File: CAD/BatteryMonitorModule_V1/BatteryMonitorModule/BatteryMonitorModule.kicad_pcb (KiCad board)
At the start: 2 copper layers, 74.6 x 74.6 mm, 72 parts, among them J1 J_FAN, J2 QT06ADP83H0000G, J3 J_NFC, J4 J_PANEL, J5 J_UART, J6 Conn_ARM_JTAG_SWD_10, J7 USB-C, K1 G5Q-14-DC12, Q1 AO4407A, Q2 AO4407A, Q3 AO3400A, Q4 MMBT2222A, Q5 2N7002, SW1 BOOT0, SW2 NRST, U1 STM32C071K8T6, U2 AP63203WU-7, U3 INA226AQDGSRQ1

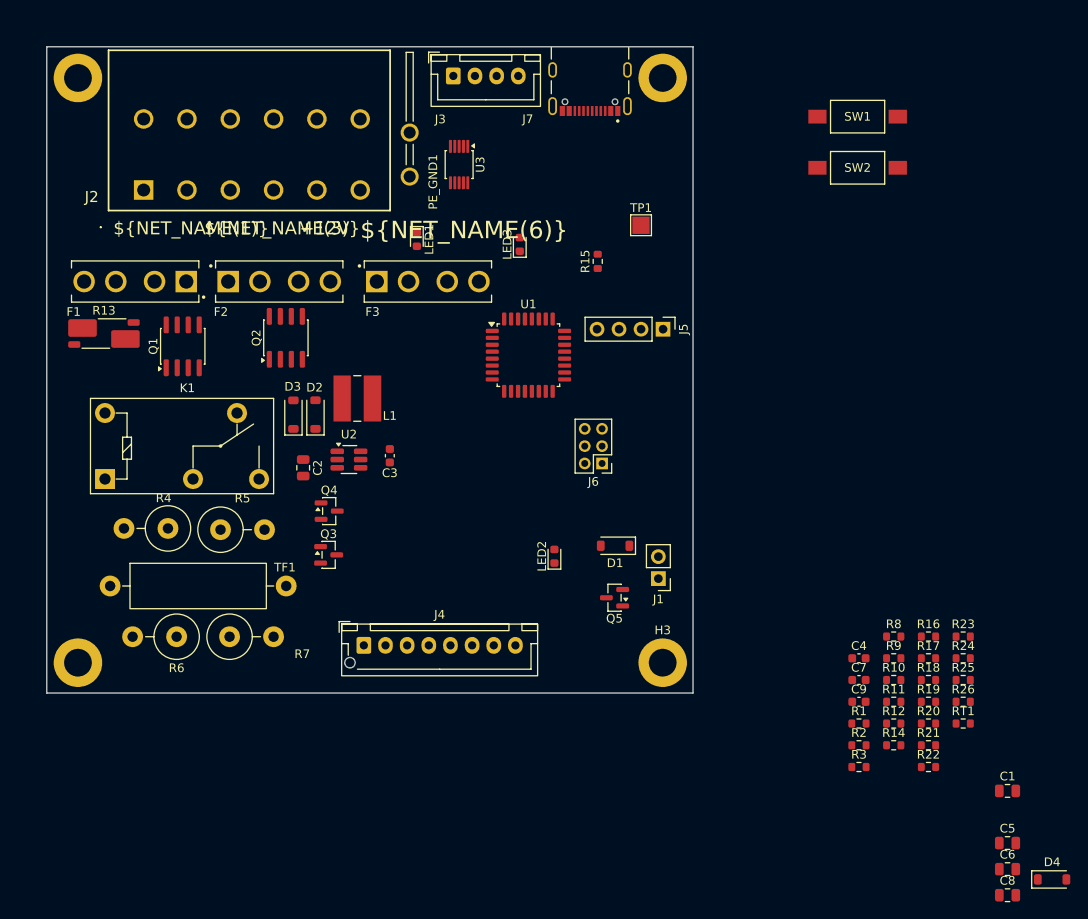
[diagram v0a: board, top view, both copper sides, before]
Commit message: V1 PCB and schematic updates
Co-Authored-By: Claude Opus 4.7 (1M context) <noreply@anthropic.com>
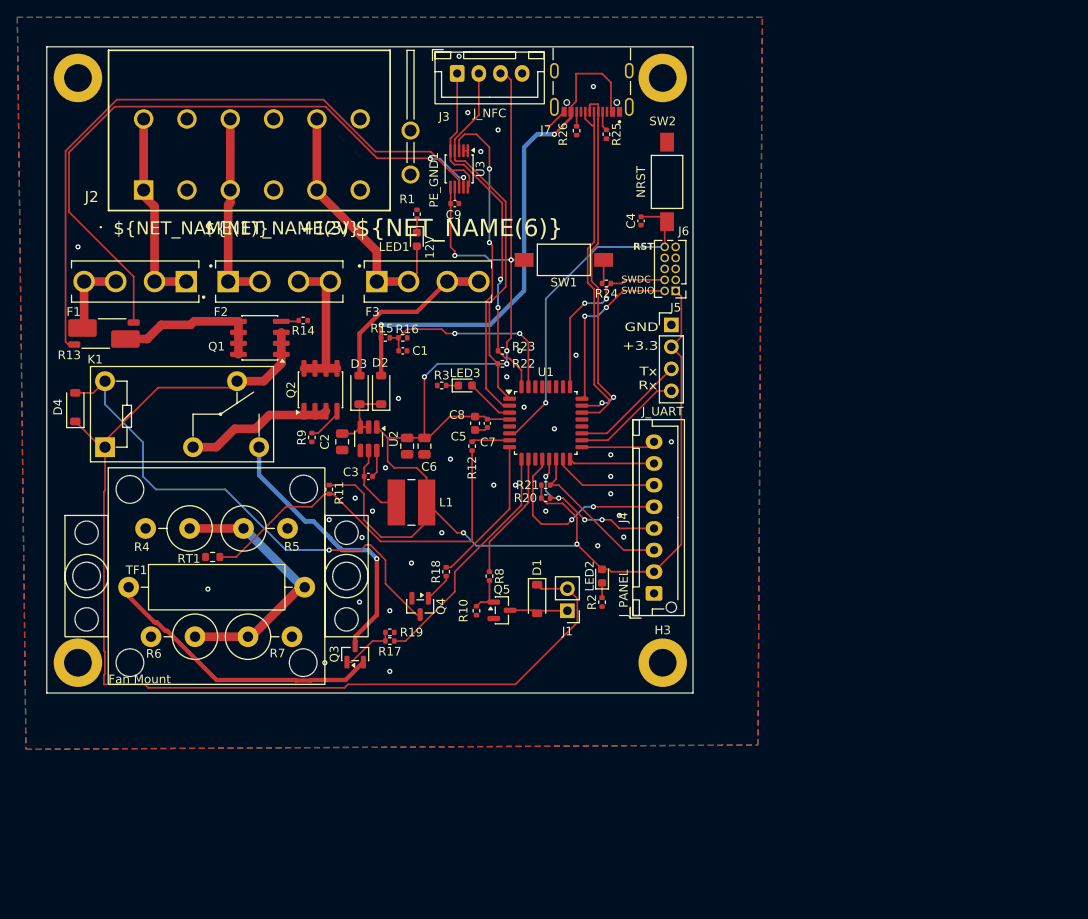
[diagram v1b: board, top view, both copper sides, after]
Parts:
- removed TP1: +3.3V, TestPoint:TestPoint_Pad_2.0x2.0mm
- added H5: Fan1, BatteryMonitorModule_Custom:2510FanOverhead, F.Cu at (45.0, 86.5)
- C1: footprint Capacitor_SMD:C_0805_2012Metric -> Capacitor_SMD:C_0402_1005Metric
- C3, C4, C7, C9: footprint Capacitor_SMD:C_0603_1608Metric -> Capacitor_SMD:C_0402_1005Metric
- C8: footprint Capacitor_SMD:C_0805_2012Metric -> Capacitor_SMD:C_0603_1608Metric
- J6: footprint Connector_PinHeader_2.00mm:PinHeader_2x03_P2.00mm_Vertical -> Connector_PinHeader_1.27mm:PinHeader_2x05_P1.27mm_Vertical
- R1: value 2k -> 10k; footprint Resistor_SMD:R_0603_1608Metric -> Resistor_SMD:R_0402_1005Metric
- R10, R11, R14, R15, R16, R17, R18, R19, R24, R25, R26, R9: footprint Resistor_SMD:R_0603_1608Metric -> Resistor_SMD:R_0402_1005Metric
- R12, R8: value 100R -> 100; footprint Resistor_SMD:R_0603_1608Metric -> Resistor_SMD:R_0402_1005Metric
- R2, R3: value 270R -> 5k1; footprint Resistor_SMD:R_0603_1608Metric -> Resistor_SMD:R_0402_1005Metric
- R20, R21, R22, R23: value 4k7 -> 5k1; footprint Resistor_SMD:R_0603_1608Metric -> Resistor_SMD:R_0402_1005Metric
- SW1, SW2: footprint BatteryMonitorModule_Custom:SWITCH_FSMSM_TYC -> Button_Switch_SMD:SW_SPST_FSMSM
- moved D4 125.2 mm to (28.7, 67.0), turned to 90 degrees
- moved RT1 88.7 mm to (44.5, 84.3), turned to 180 degrees
- moved C1 86.3 mm to (66.5, 60.5)
- moved C6 84.8 mm to (67.0, 71.5), turned to -90 degrees
- moved R14 84.0 mm to (55.0, 57.0), turned to 180 degrees
- moved C8 82.1 mm to (74.8, 68.9), turned to -90 degrees
- moved C5 81.4 mm to (69.0, 71.5), turned to -90 degrees
- moved R26 79.6 mm to (86.6, 35.1), turned to -90 degrees
- moved R1 77.8 mm to (68.1, 44.7), turned to -90 degrees
- moved R25 75.3 mm to (90.0, 35.5), turned to -90 degrees
- moved C9 74.1 mm to (72.5, 43.5)
- moved R9 71.8 mm to (56.0, 70.5), turned to 90 degrees
- moved R16 69.8 mm to (66.5, 59.0), turned to 180 degrees
- moved R11 69.6 mm to (58.0, 76.5), turned to 90 degrees
- moved R22 67.7 mm to (78.0, 62.0), turned to 180 degrees
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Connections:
- net SHUNT_N renamed SHUNT-
- net SHUNT_P renamed SHUNT+
- D1 pad 1: +BATT -> BATT+
- D2 pad 2: +5VUsb -> +5vuSB
- F1 pad 1: BATT+ -> BATT_IN+
- J1 pad 2: +BATT -> BATT+
- J2 pad 1: BATT+ -> BATT_IN+
- Q5 pad 1: FAN_PWM -> Net-(Q5-G)
- R10 pad 1: FAN_PWM -> Net-(Q5-G)
- R15 pad 2: +5VUsb -> +5vuSB
- R8 pad 2: FAN_PWM -> Net-(Q5-G)
- U1 pad 10: GPIO_K1 -> FAN_PWM
- U1 pad 11: GPIO_BLEED -> unconnected-(U1-PA4-Pad11)
- U1 pad 13: unconnected-(U1-PA6-Pad13) -> I2C2_SDA
- U1 pad 14: unconnected-(U1-PA7-Pad14) -> I2C2_SCL
- U1 pad 18: unconnected-(U1-PA8-Pad18) -> UART1_RX
- U1 pad 20: FAN_PWM -> unconnected-(U1-PC6-Pad20)
- U1 pad 21: UART1_RX -> unconnected-(U1-PA10-Pad21)
- U1 pad 3: unconnected-(U1-PC15-Pad3) -> MCU_LED
- U1 pad 30: MCU_LED -> unconnected-(U1-PB6-Pad30)
- U1 pad 8: unconnected-(U1-PA1-Pad8) -> GPIO_K1
- U1 pad 9: unconnected-(U1-PA2-Pad9) -> GPIO_BLEED
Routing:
- net +3.3V: track 0.00 -> 188.8 mm, vias 0 -> 7
- net BATT+: track 0.00 -> 127.2 mm
- net SHUNT+: track 0.00 -> 79.7 mm
- net SHUNT-: track 0.00 -> 75.1 mm, vias 0 -> 2
- net +5vuSB: track 0.00 -> 60.6 mm, vias 0 -> 2
- net Net-(D4-A): track 0.00 -> 57.5 mm, vias 0 -> 1
- net Net-(R11-Pad1): track 0.00 -> 44.9 mm
- net I2C1_SDA: track 0.00 -> 44.0 mm
- net I2C1_SCL: track 0.00 -> 41.5 mm, vias 0 -> 2
- net USB_D-: track 0.00 -> 41.0 mm, vias 0 -> 2
- net USB_D+: track 0.00 -> 40.7 mm
- net NRST: track 0.00 -> 40.1 mm, vias 0 -> 1
- net INA_ALERT: track 0.00 -> 37.5 mm, vias 0 -> 2
- net /Load_Bank: track 0.00 -> 33.3 mm
- net Net-(Q3-D): track 0.00 -> 31.9 mm, vias 0 -> 1
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- added copper zone on B.Cu, net GND
- added copper zone on F.Cu, net GND
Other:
- board text added: "+3.3"
- board text added: "12V"
- board text added: "GND"
- board text added: "RST"
- board text added: "SWDC SWDIO"
- board text added: "Tx Rx"

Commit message: finalize BatteryMonitorModule V1: pcb/sch updates, JST XH 8-pin footprint, gerber export
Co-Authored-By: Claude Opus 4.7 (1M context) <noreply@anthropic.com>
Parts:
- added FID1: Fiducial, Fiducial:Fiducial_0.5mm_Mask1.5mm, F.Cu at (28.9, 34.6)
- added FID2: Fiducial, Fiducial:Fiducial_0.5mm_Mask1.5mm, F.Cu at (93.8, 92.5)
- added FID3: Fiducial, Fiducial:Fiducial_0.5mm_Mask1.5mm, F.Cu at (86.2, 40.0)
- added J8: J_PANEL, Connector_PinHeader_2.54mm:PinHeader_2x03_P2.54mm_Vertical, F.Cu at (85.4, 97.7)
- moved SW1 1.91 mm to (87.0, 50.0)
- moved R24 1.00 mm to (91.0, 52.7)
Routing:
- net SW_A: track 22.2 -> 47.6 mm
- net SW_B: track 12.2 -> 35.1 mm
- net I2C2_SCL: track 18.4 -> 35.5 mm, vias 0 -> 1
- net I2C2_SDA: track 19.8 -> 35.6 mm
- net +3.3V: track 188.8 -> 201.9 mm
- net USB_D-: track 41.0 -> 39.8 mm
- net BOOT0/SWDCLK: track 21.4 -> 20.9 mm
- net GND: vias 35 -> 37
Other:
- board text added: "Battery Charger Monitor Module github.com/ tuffinmuffin/battery-cart V2 Rev -"
- board text added: "WayWayWay"
